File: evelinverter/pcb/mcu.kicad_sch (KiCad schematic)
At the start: 9 parts, among them U1 STM32G071CBU3, Y1 RH100-8

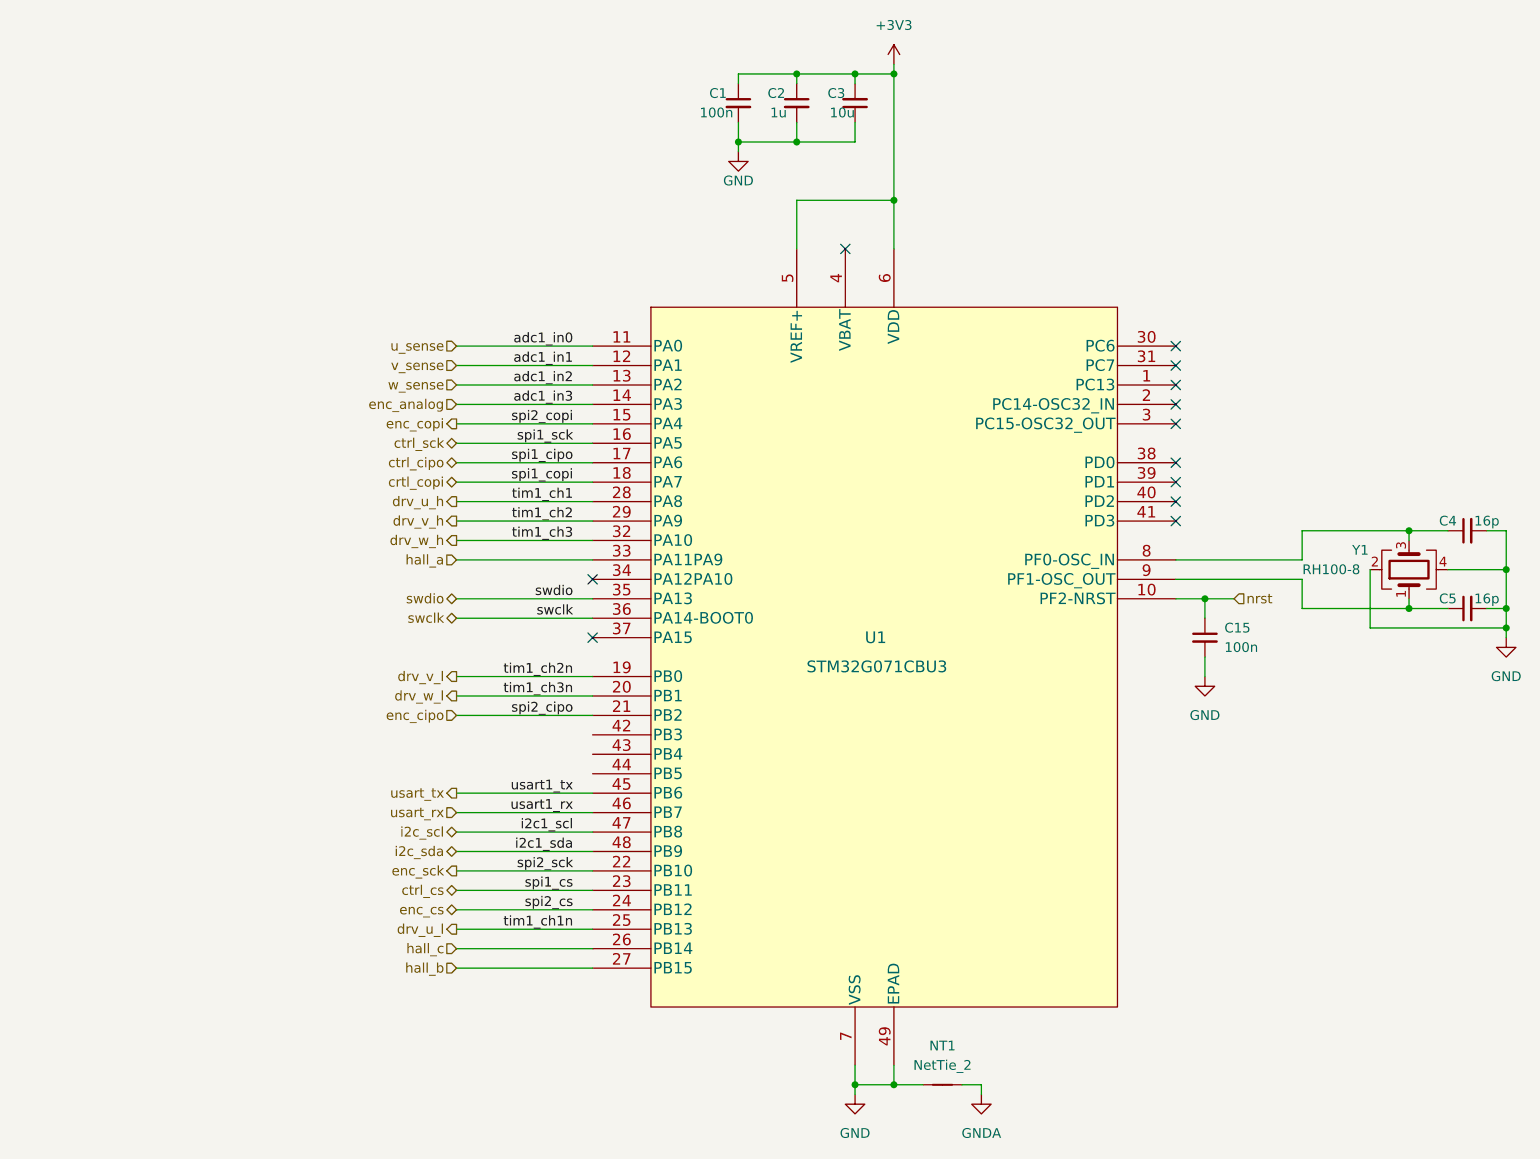
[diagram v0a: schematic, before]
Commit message: started redoing evelinverter
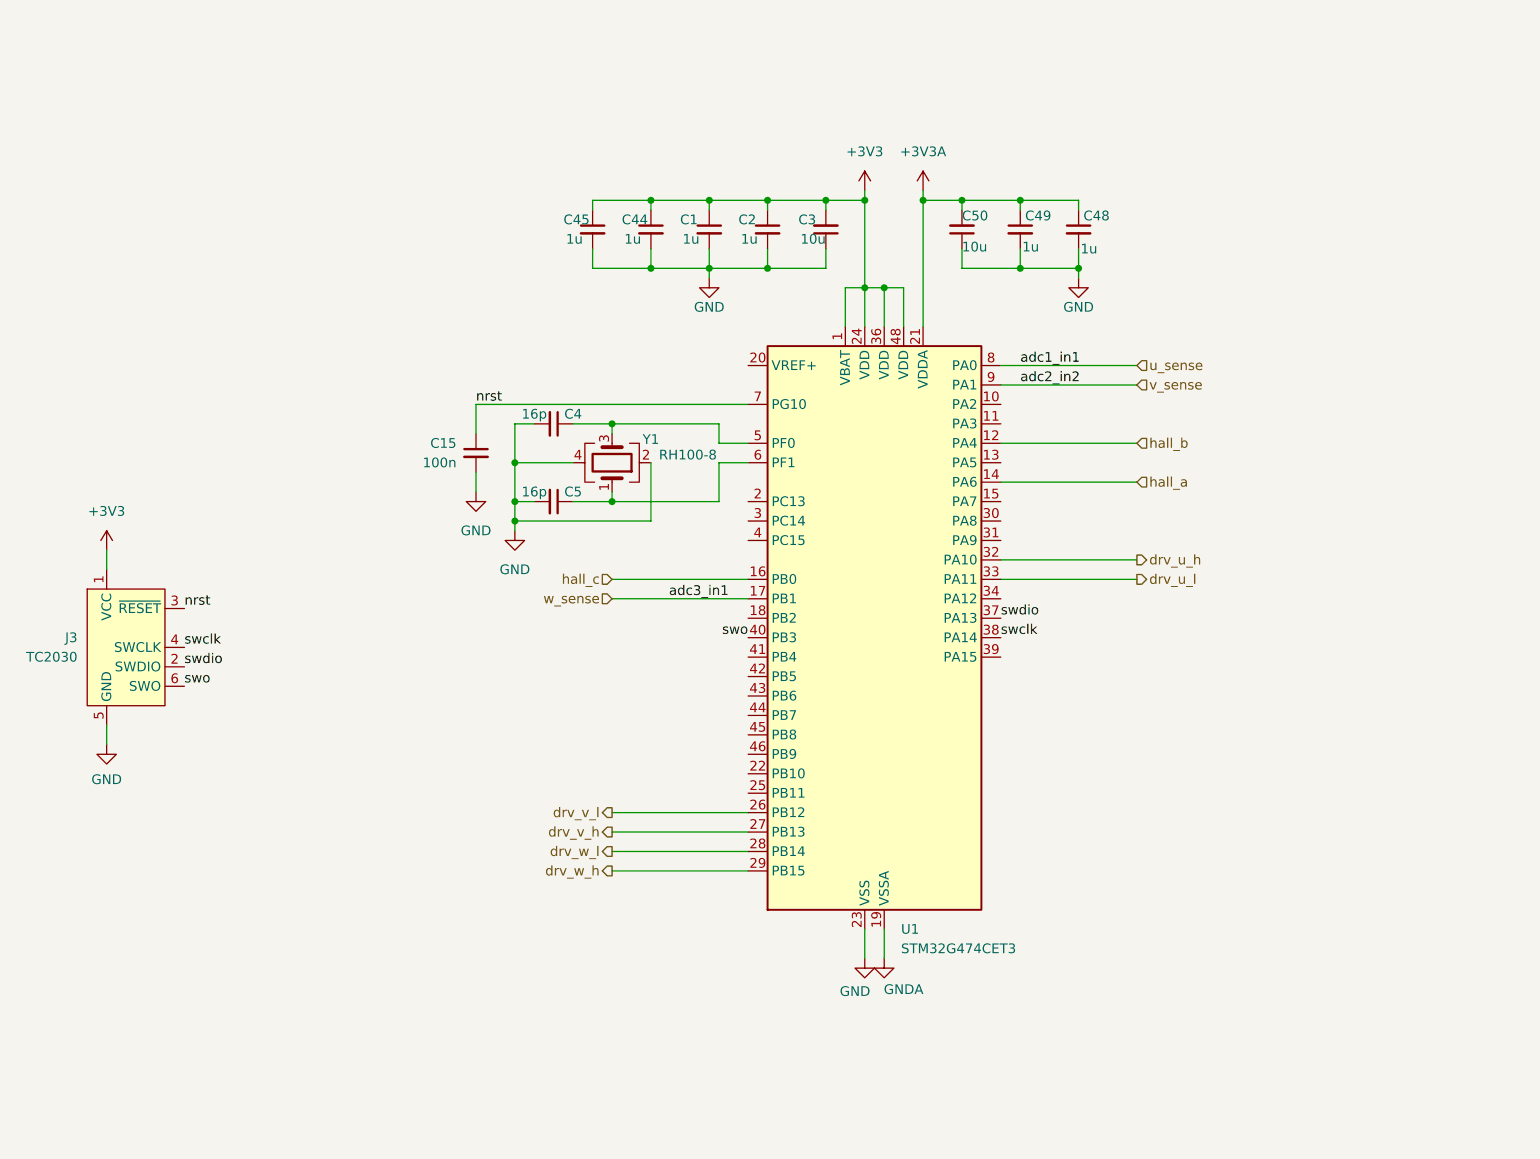
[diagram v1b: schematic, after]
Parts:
- removed NT1: NetTie_2, NetTie:NetTie-2_SMD_Pad0.5mm, symbol Device:NetTie_2
- removed U1: STM32G071CBU3, Package_DFN_QFN:QFN-48-1EP_7x7mm_P0.5mm_EP5.45x5.45mm, symbol a22verter:STM32G071CBU3
- added C44, C45, C48, C49: 1u, Capacitor_SMD:C_0402_1005Metric, symbol Device:C_Small
- added C50: 10u, Capacitor_SMD:C_0402_1005Metric, symbol Device:C_Small
- added J3: TC2030, Connector:Tag-Connect_TC2030-IDC-NL_2x03_P1.27mm_Vertical, symbol Connector:Conn_ARM_SWD_TagConnect_TC2030
- added U1: STM32G474CET3, Package_QFP:LQFP-48_7x7mm_P0.5mm, symbol #inventree:STM32G474CET3
- C1: value 100n -> 1u
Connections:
- net +3V3: now also C44.1, C45.1, J3.1 (VCC), U1.1 (VBAT), U1.24 (VDD), U1.36 (VDD), U1.48 (VDD)
- net GND: now also C44.2, C45.2, C48.2, C49.2, C50.1, J3.5 (GND), U1.23 (VSS), U1.35 (VSS), U1.47 (VSS)
- net GNDA: now also U1.19 (VSSA)
- net drv_u_h: now also U1.32 (PA10)
- net drv_u_l: now also U1.33 (PA11)
- net drv_v_h: now also U1.27 (PB13)
- net drv_v_l: now also U1.26 (PB12)
- net drv_w_h: now also U1.29 (PB15)
- net drv_w_l: now also U1.28 (PB14)
- net hall_a: now also U1.14 (PA6)
- net hall_b: now also U1.12 (PA4)
- net hall_c: now also U1.16 (PB0)
- net nrst: now also J3.3 (~{RESET}), U1.7 (PG10)
- net swclk: now also J3.4 (SWCLK), U1.38 (PA14)
- net swdio: now also J3.2 (SWDIO), U1.37 (PA13)
- net u_sense: now also U1.8 (PA0)
- net v_sense: now also U1.9 (PA1)
- net w_sense: now also U1.17 (PB1)
- net at C4.1, Y1.3: now also U1.5 (PF0)
- net at C5.1, Y1.1: now also U1.6 (PF1)
- new net +3V3A: C48.1, C49.1, C50.2, U1.21 (VDDA)
- new net swo: J3.6 (SWO), U1.40 (PB3)
- no-connect marks 12 -> 0
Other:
- moved on the sheet: C15, C2, C3, C4, C5, Y1
